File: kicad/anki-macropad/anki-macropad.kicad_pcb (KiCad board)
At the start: 2 copper layers, 46 parts, among them J1 USB_C_Receptacle_USB2.0_14P, SW1 PTS810 SJK 250 SMTR LFS, U1 RP2040, U2 NCP1117-3.3_SOT223, U3 W25Q128JVS, U4 USBLC6-2SC6, X1 ABM8-272-T3

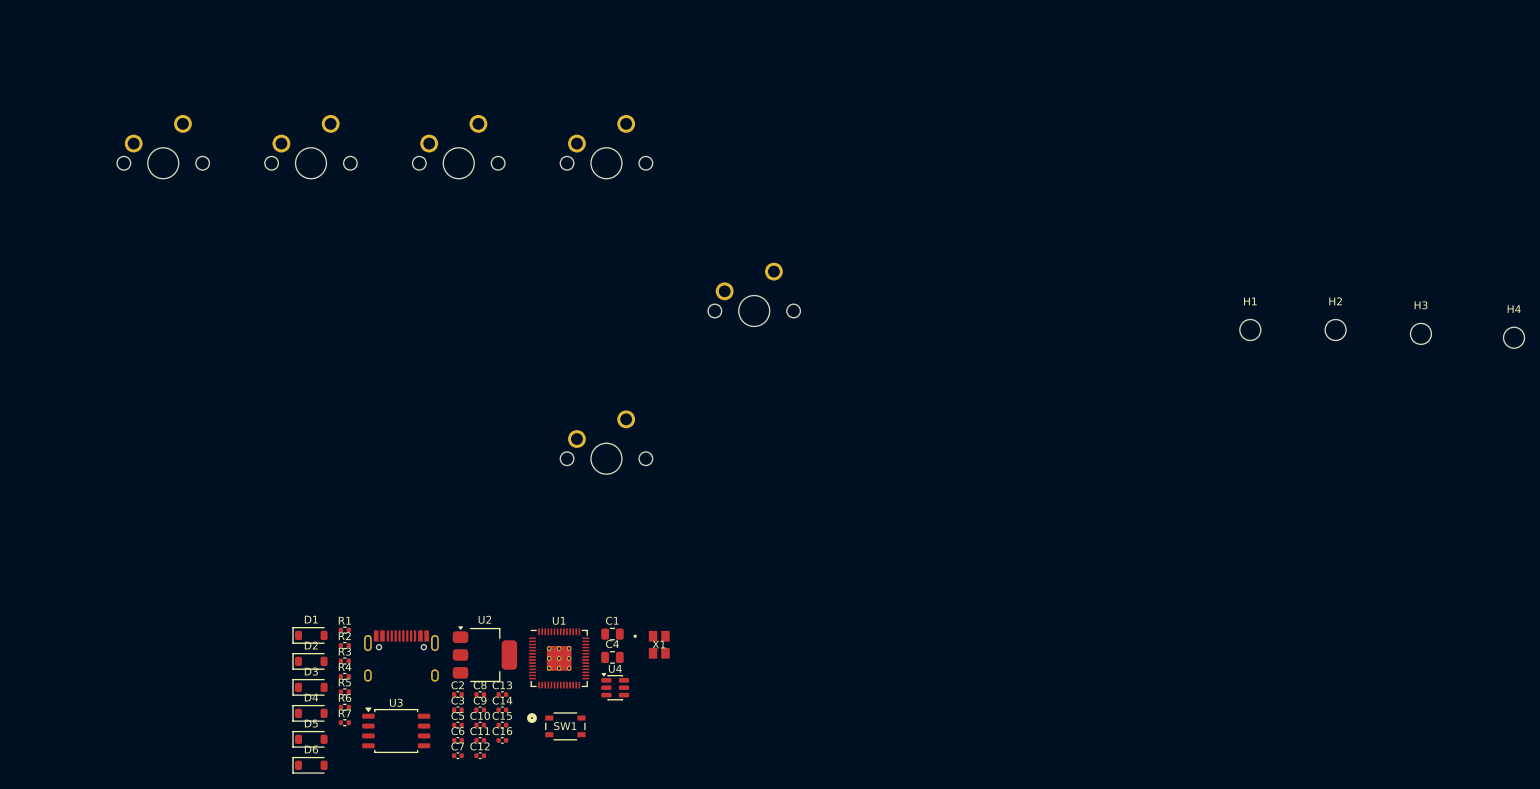
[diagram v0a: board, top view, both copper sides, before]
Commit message: Worked on PCB layout and traces
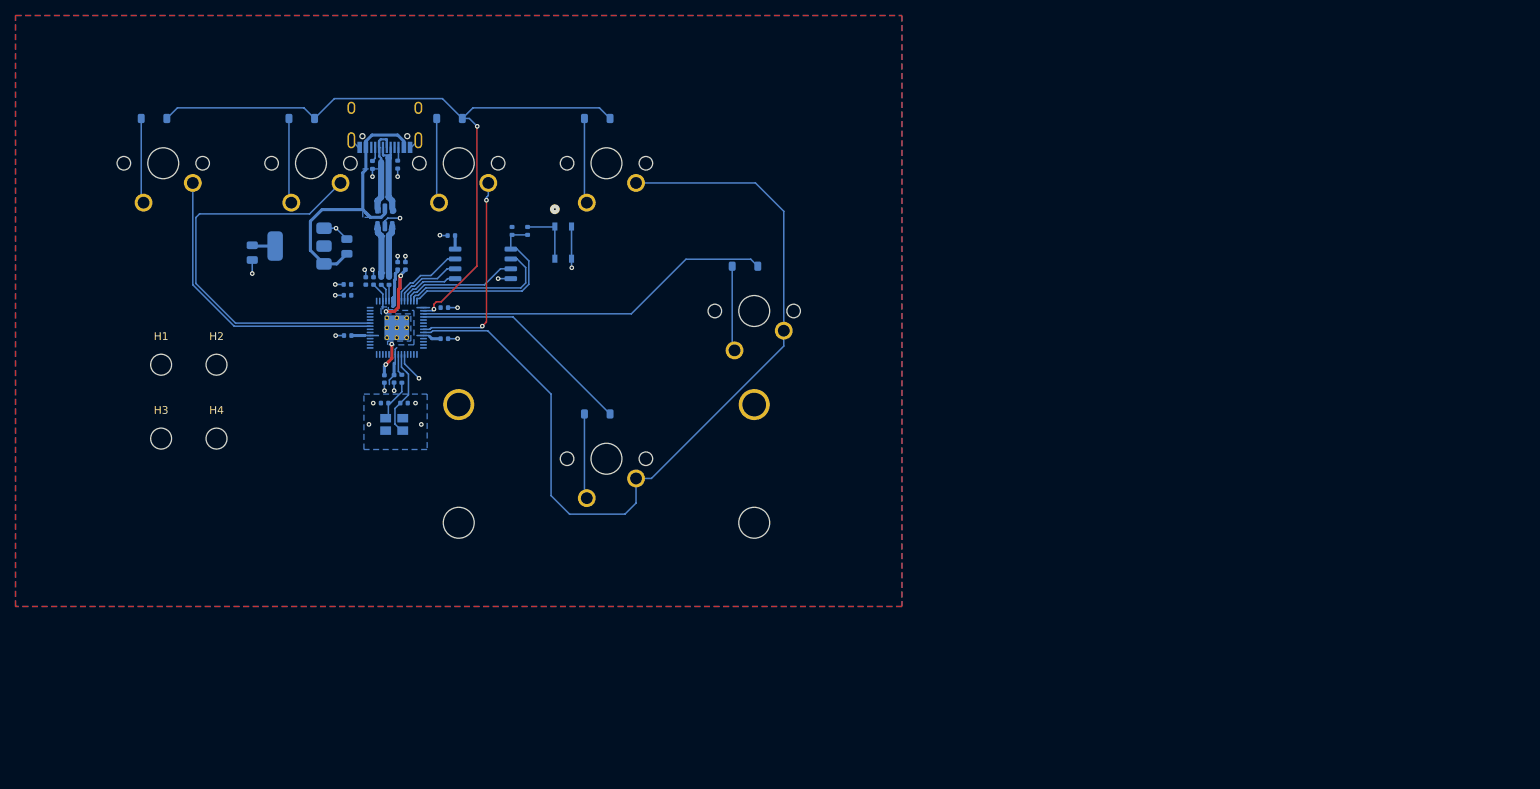
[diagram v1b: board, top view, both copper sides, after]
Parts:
- added REF**: STAB_MX_P_3u, PCM_marbastlib-mx:STAB_MX_P_3u, F.Cu at (114.0, 83.1)
- C1, C10, C11, C12, C13, C14, C15, C16, C2, C3, C4, C5, C6, C7, C8, C9, D1, D2, D3, D4, D5, D6, J1, R1, R2, R3, R4, R5, R6, R7, SW1, U4, X1: moved to B.Cu
- U1: renamed from U2; moved to B.Cu
- U2: renamed from U3; moved to B.Cu
- U3: renamed from U1; moved to B.Cu
- moved H4 167.8 mm to (63.7, 80.5)
- moved H3 163.0 mm to (56.6, 80.5)
- moved H2 144.4 mm to (63.7, 71.0)
- moved H1 140.5 mm to (56.6, 71.0)
- moved D4 85.1 mm to (112.8, 39.2), turned to 180 degrees
- moved D5 82.8 mm to (131.8, 58.3), turned to 180 degrees
- moved D3 75.5 mm to (93.7, 39.2), turned to 180 degrees
- moved R7 72.3 mm to (87.1, 45.2), turned to -90 degrees
- moved J1 71.1 mm to (85.4, 38.9)
- moved R6 70.0 mm to (83.8, 45.2), turned to -90 degrees
- moved D2 70.0 mm to (74.7, 39.2), turned to 180 degrees
- moved C4 69.9 mm to (68.3, 56.5), turned to -90 degrees
- moved D1 69.7 mm to (55.6, 39.2), turned to 180 degrees
- moved U4 67.5 mm to (85.4, 52.0), turned to 90 degrees
- moved C5 63.1 mm to (94.0, 54.3), turned to 180 degrees
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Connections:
- J1 pad S1: (no net) -> GND
- R3 pad 1: Net-(U1-USB_DP) -> /MCU_D+
- R3 pad 2: /MCU_D+ -> Net-(U3-USB_DP)
- R7 pad 1: GND -> Net-(J1-CC2)
- R7 pad 2: Net-(J1-CC2) -> GND
- U3 pad 36: unconnected-(U1-GPIO24-Pad36) -> /COLUMN 0
- U3 pad 37: unconnected-(U1-GPIO25-Pad37) -> /COLUMN 1
- U3 pad 47: Net-(U1-USB_DP) -> Net-(U3-USB_DP)
- U3 pad 6: /COLUMN 0 -> unconnected-(U3-GPIO4-Pad6)
- U3 pad 7: /COLUMN 1 -> unconnected-(U3-GPIO5-Pad7)
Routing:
- net /COLUMN 3: track 0.00 -> 112.8 mm
- net /ROW 0: track 0.00 -> 91.6 mm, vias 0 -> 2
- net /COLUMN 1: track 0.00 -> 53.5 mm
- net /ROW 1: track 0.00 -> 46.4 mm
- net /COLUMN 0: track 0.00 -> 38.2 mm
- net VBUS: track 0.00 -> 37.4 mm
- net GND: track 0.00 -> 36.2 mm, vias 0 -> 24
- net /ROW 2: track 0.00 -> 29.2 mm
- net /COLUMN 2: track 0.00 -> 26.5 mm, vias 0 -> 2
- net /QSPI_SS: track 0.00 -> 25.4 mm
- net +3V3: track 0.00 -> 25.4 mm
- net +1V1: track 0.00 -> 20.3 mm, vias 0 -> 4
- net /QSPI_SD1: track 0.00 -> 20.1 mm
- net /QSPI_SD2: track 0.00 -> 15.0 mm
- net /XIN: track 0.00 -> 11.4 mm
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- added copper zone on B.Cu, net +1V1
- added copper zone on B.Cu, net +3V3
- added copper zone on B.Cu, net GND
- added copper zone on F.Cu, net GND

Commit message: Pretty much finished the PCB. Just need to go through DRC.
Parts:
- added G***: LOGO, OP:g5, F.Cu at (54.0, 89.1)
- H1, H2, H3, H4: value MountingHole -> MountingHole_Pad; footprint MountingHole:MountingHole_2.7mm_M2.5 -> MountingHole:MountingHole_2.7mm_M2.5_Pad
- moved H2 76.0 mm to (134.6, 43.5)
- moved H3 63.8 mm to (119.6, 70.6)
- moved H1 12.6 mm to (55.3, 58.5)
- moved H4 6.61 mm to (70.3, 80.6)
- moved C11 0.90 mm to (94.0, 63.5)
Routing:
- net +3V3: track 25.4 -> 28.9 mm
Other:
- board outline added: 99.2 x 62.1 mm

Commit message: Update anki-macropad.kicad_pcb
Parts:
- moved G*** 0.78 mm to (53.5, 89.7)
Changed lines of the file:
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@@
 		(capping no)
 		(filling no)
-		(zone_defaults)
 		(grid_origin 144.557499 33.475)
 		(pcbplotparams
@@
 	(footprint "OP:g5"
 		(layer "F.Cu")
-		(at 53.967499 89.115)
+		(at 53.461079 89.702346)
 		(property "Reference" "G***"
 			(at 0 0 0)

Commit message: Finished PCB design including DRC
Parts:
- moved J1 1.84 mm to (85.4, 37.1)
- moved R6 1.80 mm to (83.8, 43.4)
- moved R7 1.79 mm to (87.1, 43.4)
- moved C2 0.36 mm to (87.9, 76.3)
- moved C3 0.36 mm to (85.4, 76.3)
- moved X1 0.36 mm to (86.6, 79.0)
- turned R3 to -90 degrees
- turned R4 to -90 degrees
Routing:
- net /USB_D-: track 11.1 -> 13.0 mm
- net /USB_D+: track 9.88 -> 11.6 mm
- net GND: track 36.2 -> 34.9 mm
- net /ROW 0: track 91.6 -> 90.7 mm

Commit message: Made final touches to PCB. Ordered.
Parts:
- removed G***: LOGO, OP:g5
